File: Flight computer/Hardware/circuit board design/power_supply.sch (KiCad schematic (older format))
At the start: 0 parts

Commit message: Got the GPS wired up with the MAX-M8C.
I wired up the MCU to the GPS as well. Sensors are also wired up to the I2C line.

TODO:
-make everything run on 3.3V
- work out the pyro charges and drivers
many more.
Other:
- note added: "Figure out how to use a linear power supply with a 3.7 V lithium cell\n"
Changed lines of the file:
@@
 $Descr A4 11693 8268
 encoding utf-8
-Sheet 5 6
+Sheet 3 6
 Title ""
 Date ""
@@
 Comment4 ""
 $EndDescr
+Text Notes 6700 5500 0    50   ~ 0
+Figure out how to use a linear power supply with a 3.7 V lithium cell\n
 $EndSCHEMATC

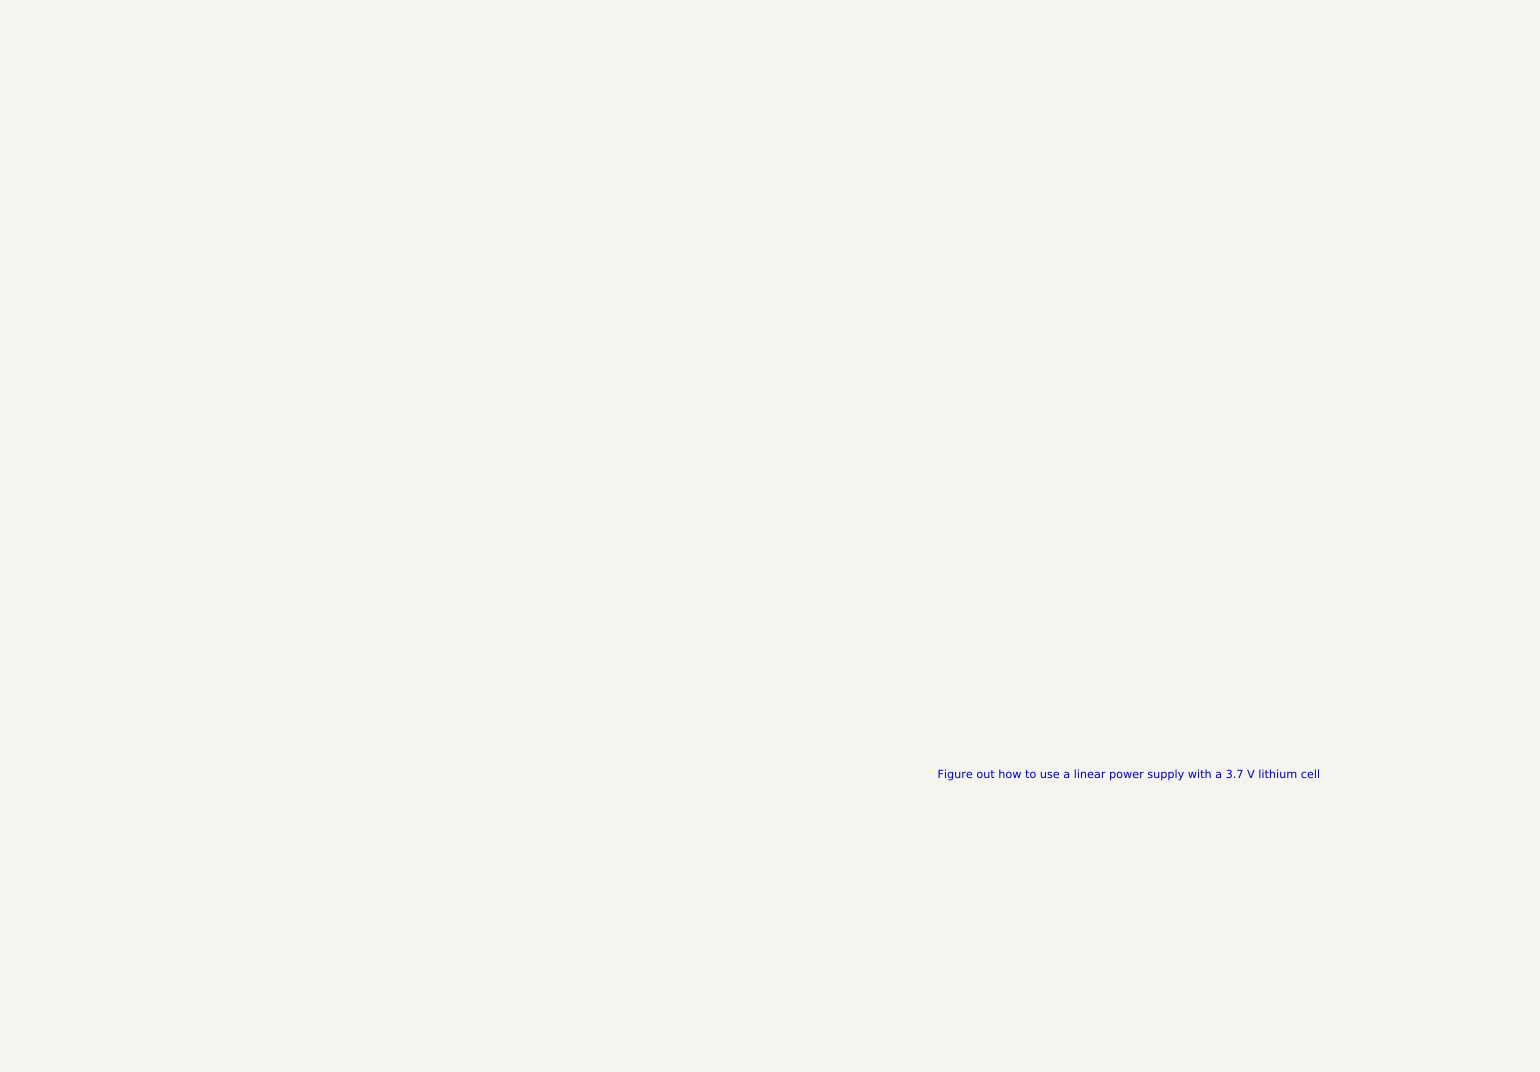
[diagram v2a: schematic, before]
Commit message: changed boost converter resistor values for 3.3V and more
-started the pyro drivers
- connected the SPI connection between radio and MCU
- boost converter values changed.
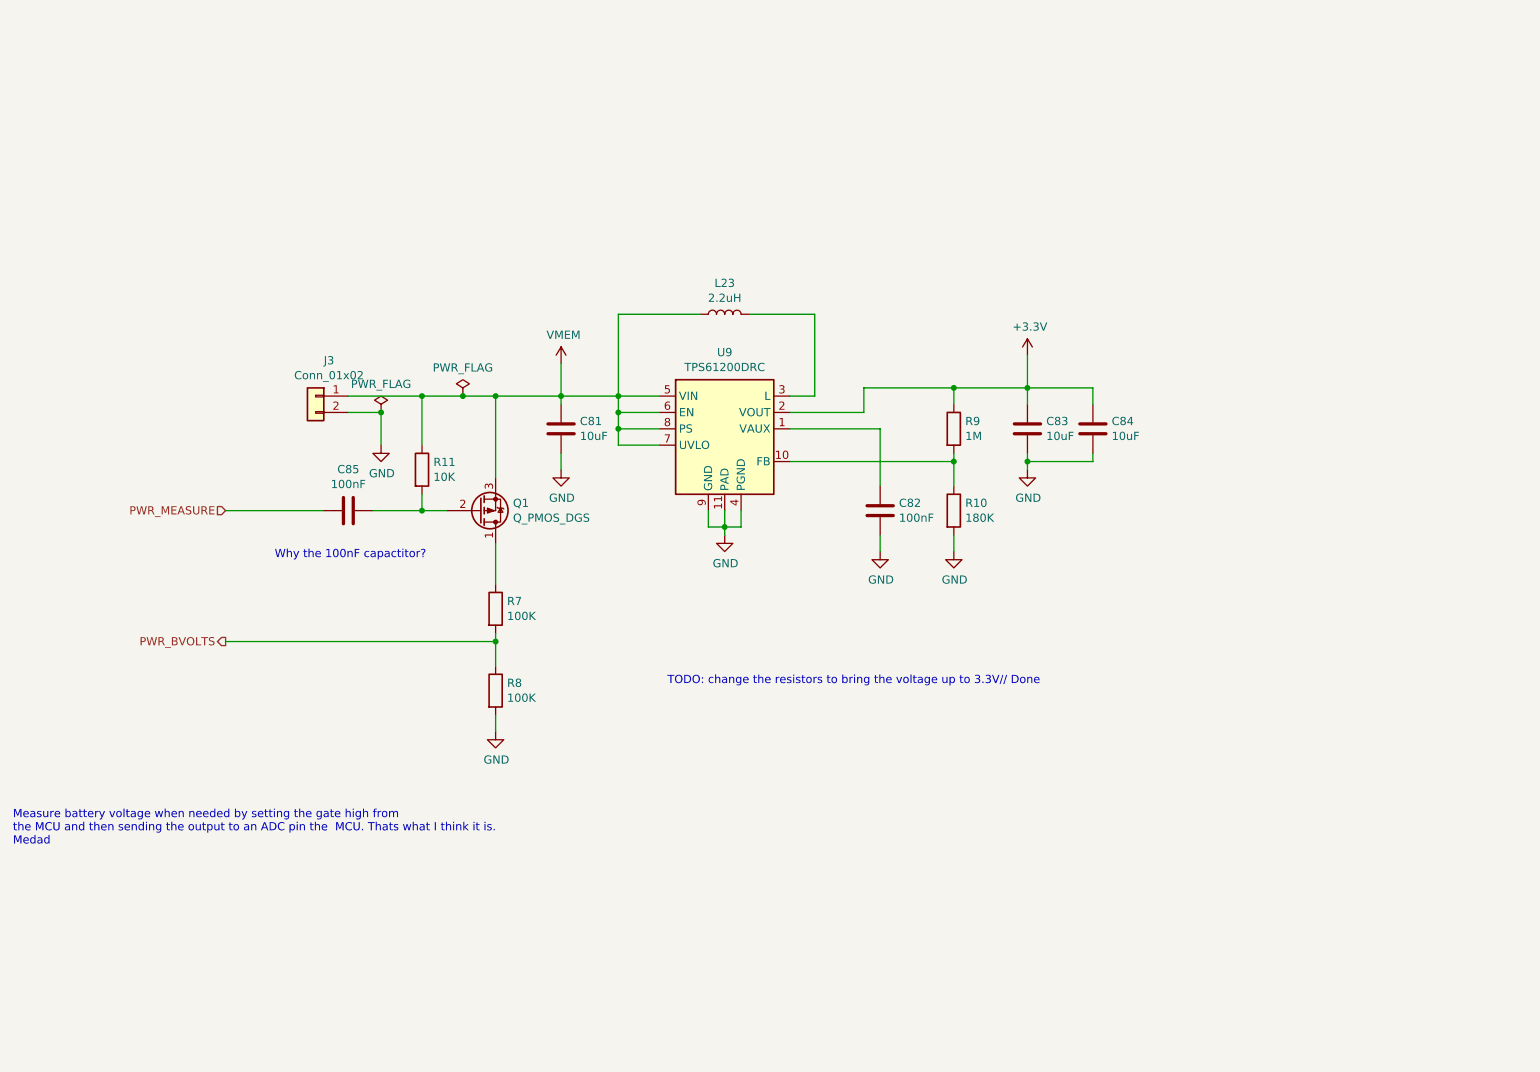
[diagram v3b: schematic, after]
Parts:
- added C81, C83, C84: 10uF, Capacitor_SMD:C_0603_1608Metric, symbol Device:C
- added C82, C85: 100nF, Capacitor_SMD:C_0603_1608Metric, symbol Device:C
- added J3: Conn_01x02, Connector_PinHeader_1.00mm:PinHeader_1x02_P1.00mm_Vertical, symbol Connector_Generic:Conn_01x02
- added L23: 2.2uH, Inductor_SMD:L_Taiyo-Yuden_NR-30xx, symbol Device:L
- added Q1: Q_PMOS_DGS, Package_TO_SOT_SMD:SOT-23, symbol Device:Q_PMOS_DGS
- added R10: 180K, Resistor_SMD:R_0603_1608Metric, symbol Device:R
- added R11: 10K, Resistor_SMD:R_0603_1608Metric, symbol Device:R
- added R7, R8: 100K, Resistor_SMD:R_0603_1608Metric, symbol Device:R
- added R9: 1M, Resistor_SMD:R_0603_1608Metric, symbol Device:R
- added U9: TPS61200DRC, Package_SON:Texas_S-PVSON-N10_ThermalVias, symbol Regulator_Switching:TPS61200DRC
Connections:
- new net: C82.1, U9.1 (VAUX)
- new net: R10.1, R9.2, U9.10 (FB)
- new net: L23.2, U9.3 (L)
- new net: Q1.1 (D), R7.1
- new net: C85.2, Q1.2 (G), R11.2
- new net +3V3: C83.1, C84.1, R9.1, U9.2 (VOUT)
- new net GND: C81.2, C82.2, C83.2, C84.2, J3.2 (Pin_2), R10.2, R8.2, U9.11 (PAD), U9.4 (PGND), U9.9 (GND)
- new net PWR_BVOLTS: R7.2, R8.1
- new net PWR_MEASURE: C85.1
- new net VMEM: C81.1, J3.1 (Pin_1), L23.1, Q1.3 (S), R11.1, U9.5 (VIN), U9.6 (EN), U9.7 (UVLO), U9.8 (PS)
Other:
- note added: "Measure battery voltage when needed by setting the gate high from \nthe MCU and then sending the output to an ADC pin the MCU. Thats what I think it is. \nMedad\n"
- note added: "TODO: change the resistors to bring the voltage up to 3.3V// Done\n\n"
- note added: "Why the 100nF capactitor?"
- note removed: "Figure out how to use a linear power supply with a 3.7 V lithium cell\n"

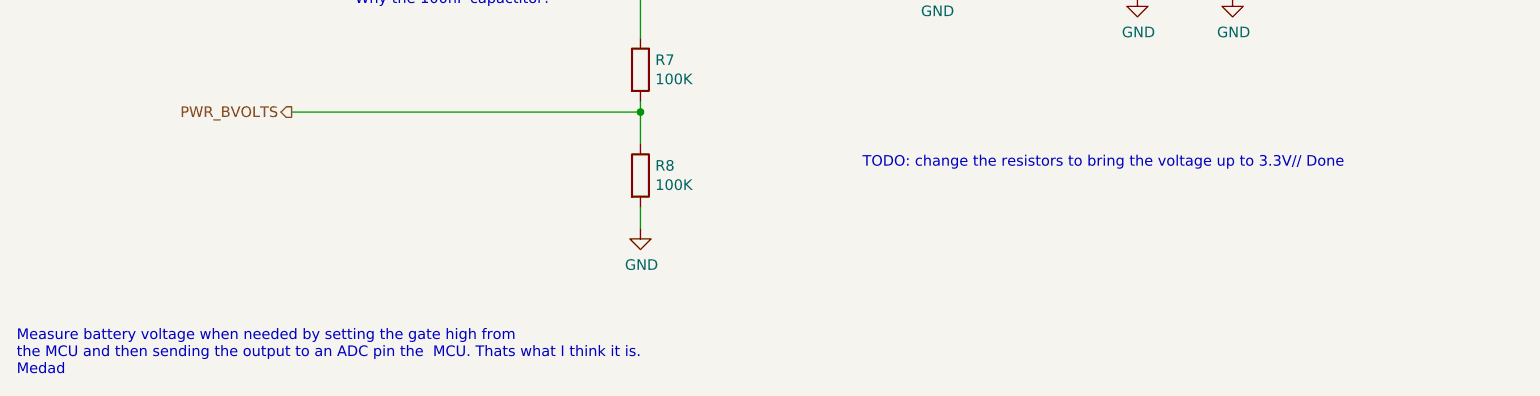
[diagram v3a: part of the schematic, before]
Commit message: more upgrades
- removed the comparators
- added the cost and link to buy components
- added in a symbol for USB
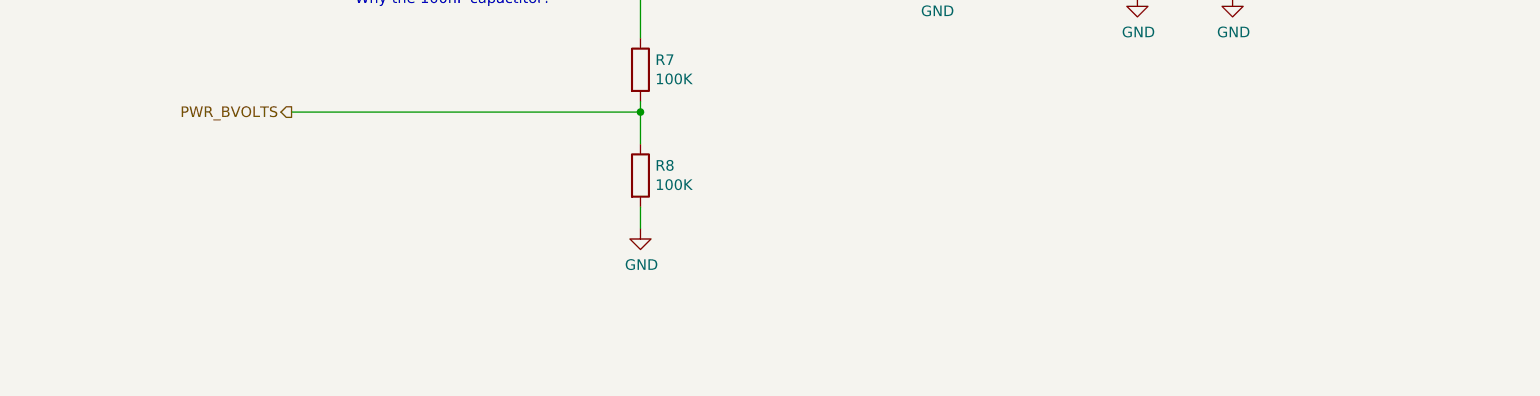
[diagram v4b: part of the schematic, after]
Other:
- note removed: "Measure battery voltage when needed by setting the gate high from \nthe MCU and then sending the output to an ADC pin the MCU. Thats what I think it is. \nMedad\n"
- note removed: "TODO: change the resistors to bring the voltage up to 3.3V// Done\n\n"
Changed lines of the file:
@@
 Wire Wire Line
 	3800 3150 4000 3150
-$Comp
-L power:PWR_FLAG #FLG0104
-U 1 1 5D62CCB0
-P 3300 3250
-F 0 "#FLG0104" H 3300 3325 50  0001 C CNN
-F 1 "PWR_FLAG" H 3300 3423 50  0000 C CNN
-F 2 "" H 3300 3250 50  0001 C CNN
-F 3 "~" H 3300 3250 50  0001 C CNN
-	1    3300 3250
-	1    0    0    -1
-$EndComp
-Connection ~ 3300 3250
 Wire Wire Line
 	6250 3100 6800 3100
-Text Notes 5050 5000 0    50   ~ 0
-TODO: change the resistors to bring the voltage up to 3.3V// Done\n\n
 Wire Wire Line
 	7250 3100 7250 2900
@@
 	1    0    0    -1
 $EndComp
-Text Notes 1050 5900 0    50   ~ 0
-Measure battery voltage when needed by setting the gate high from \nthe MCU and then sending the output to an ADC pin the  MCU. Thats what I think it is. \nMedad\n
 Text Notes 2650 4150 0    50   ~ 0
 Why the 100nF capactitor?
+Connection ~ 3300 3250
+$Comp
+L power:PWR_FLAG #FLG0104
+U 1 1 5D62CCB0
+P 3300 3250
+F 0 "#FLG0104" H 3300 3325 50  0001 C CNN
+F 1 "PWR_FLAG" H 3300 3423 50  0000 C CNN
+F 2 "" H 3300 3250 50  0001 C CNN
+F 3 "~" H 3300 3250 50  0001 C CNN
+	1    3300 3250
+	1    0    0    -1
+$EndComp
 $EndSCHEMATC

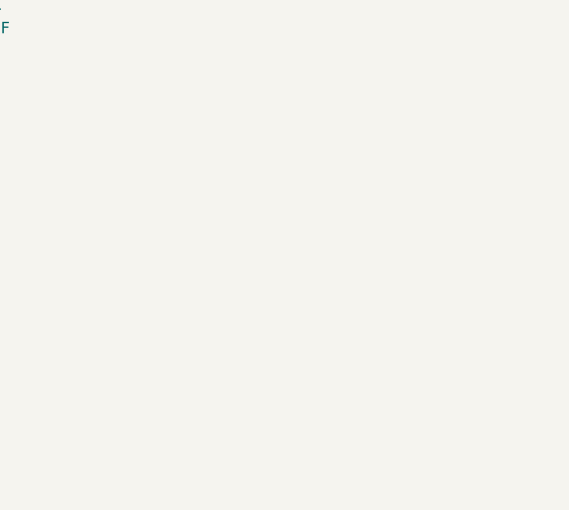
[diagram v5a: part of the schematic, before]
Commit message: moved the USB connector to power_supply schematic
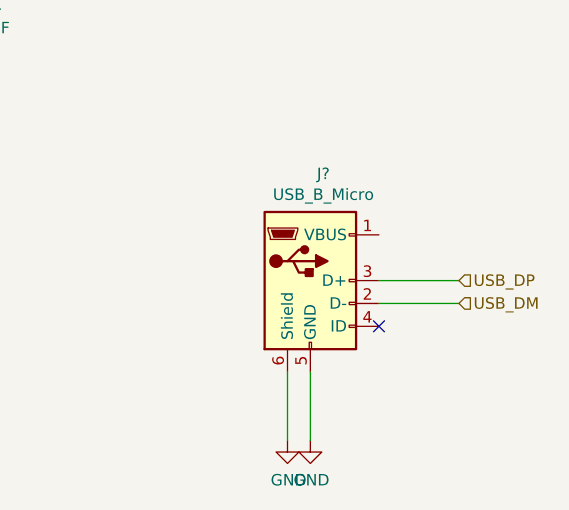
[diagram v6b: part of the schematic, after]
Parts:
- added J?: USB_B_Micro, Connector_USB:USB_Micro-B_Molex-105017-0001, symbol Connector:USB_B_Micro
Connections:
- net GND: now also J?.5 (GND), J?.6 (Shield)
- new net USB_DM: J?.2 (D-)
- new net USB_DP: J?.3 (D+)
- no-connect marks 0 -> 1
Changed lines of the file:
@@
 $Descr A4 11693 8268
 encoding utf-8
-Sheet 5 7
+Sheet 4 7
 Title ""
 Date ""
@@
 Wire Wire Line
 	6250 3100 6800 3100
+NoConn ~ 9550 4700
+Wire Wire Line
+	9150 4900 9150 5200
+$Comp
+L power:GND #PWR?
+U 1 1 5D941F2E
+P 9150 5200
+F 0 "#PWR?" H 9150 4950 50  0001 C CNN
+F 1 "GND" H 9155 5027 50  0000 C CNN
+F 2 "" H 9150 5200 50  0001 C CNN
+F 3 "" H 9150 5200 50  0001 C CNN
+	1    9150 5200
+	1    0    0    -1
+$EndComp
+Wire Wire Line
+	9250 4900 9250 5200
+Wire Wire Line
+	9900 4500 9550 4500
+Wire Wire Line
+	9550 4600 9900 4600
+$Comp
+L power:GND #PWR?
+U 1 1 5D941F37
+P 9250 5200
+F 0 "#PWR?" H 9250 4950 50  0001 C CNN
+F 1 "GND" H 9255 5027 50  0000 C CNN
+F 2 "" H 9250 5200 50  0001 C CNN
+F 3 "" H 9250 5200 50  0001 C CNN
+	1    9250 5200
+	1    0    0    -1
+$EndComp
+$Comp
+L Connector:USB_B_Micro J?
+U 1 1 5D941F3D
+P 9250 4500
+F 0 "J?" H 9307 4967 50  0000 C CNN
+F 1 "USB_B_Micro" H 9307 4876 50  0000 C CNN
+F 2 "Connector_USB:USB_Micro-B_Molex-105017-0001" H 9400 4450 50  0001 C CNN
+F 3 "~" H 9400 4450 50  0001 C CNN
+	1    9250 4500
+	1    0    0    -1
+$EndComp
+Text HLabel 9900 4600 2    50   Input ~ 0
+USB_DM
+Text HLabel 9900 4500 2    50   Input ~ 0
+USB_DP
 $EndSCHEMATC
